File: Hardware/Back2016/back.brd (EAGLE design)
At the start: 160 x 100 mm, 12 parts, among them J1 RASPBERRYPI-40-PIN-GPIO-SMT

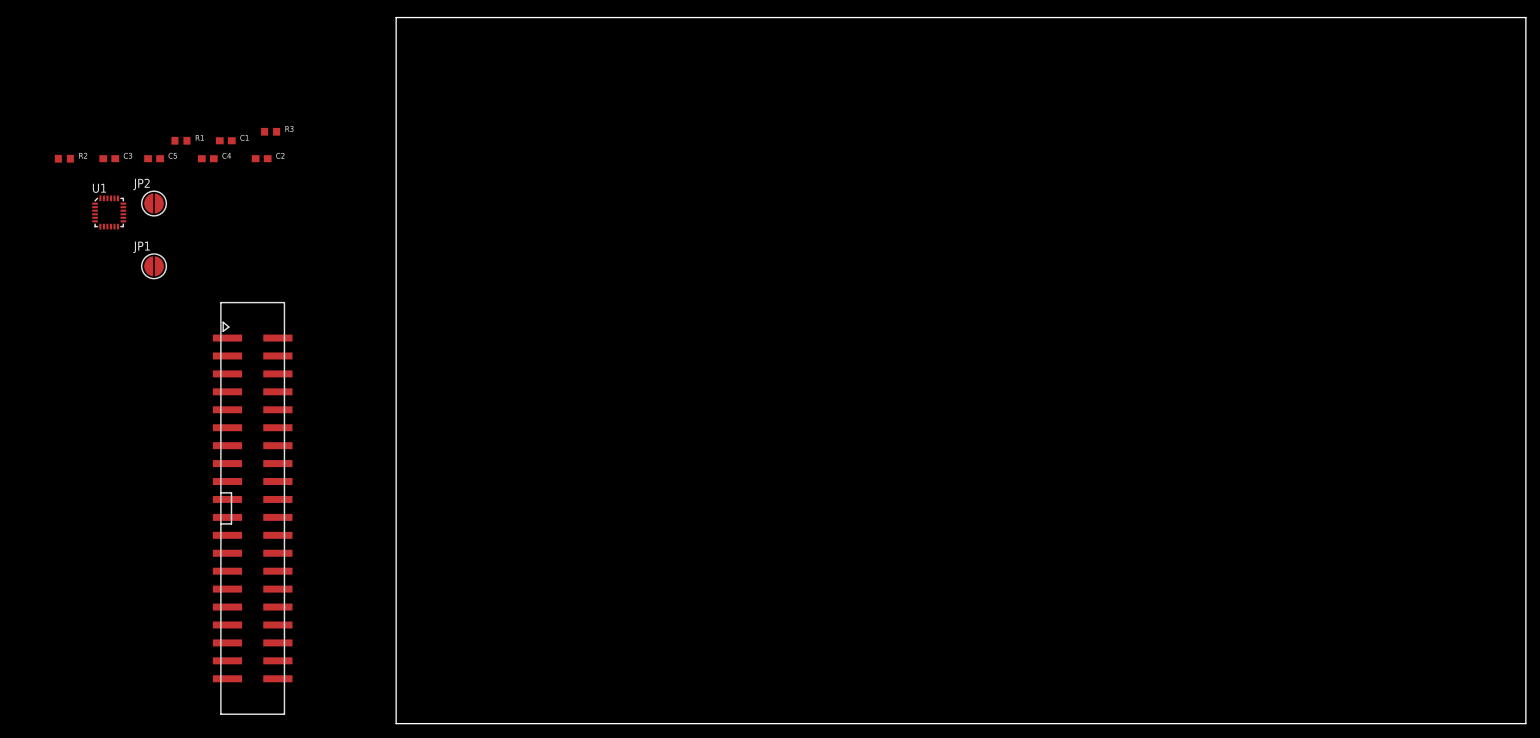
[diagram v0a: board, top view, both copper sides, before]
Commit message: Added Audio out
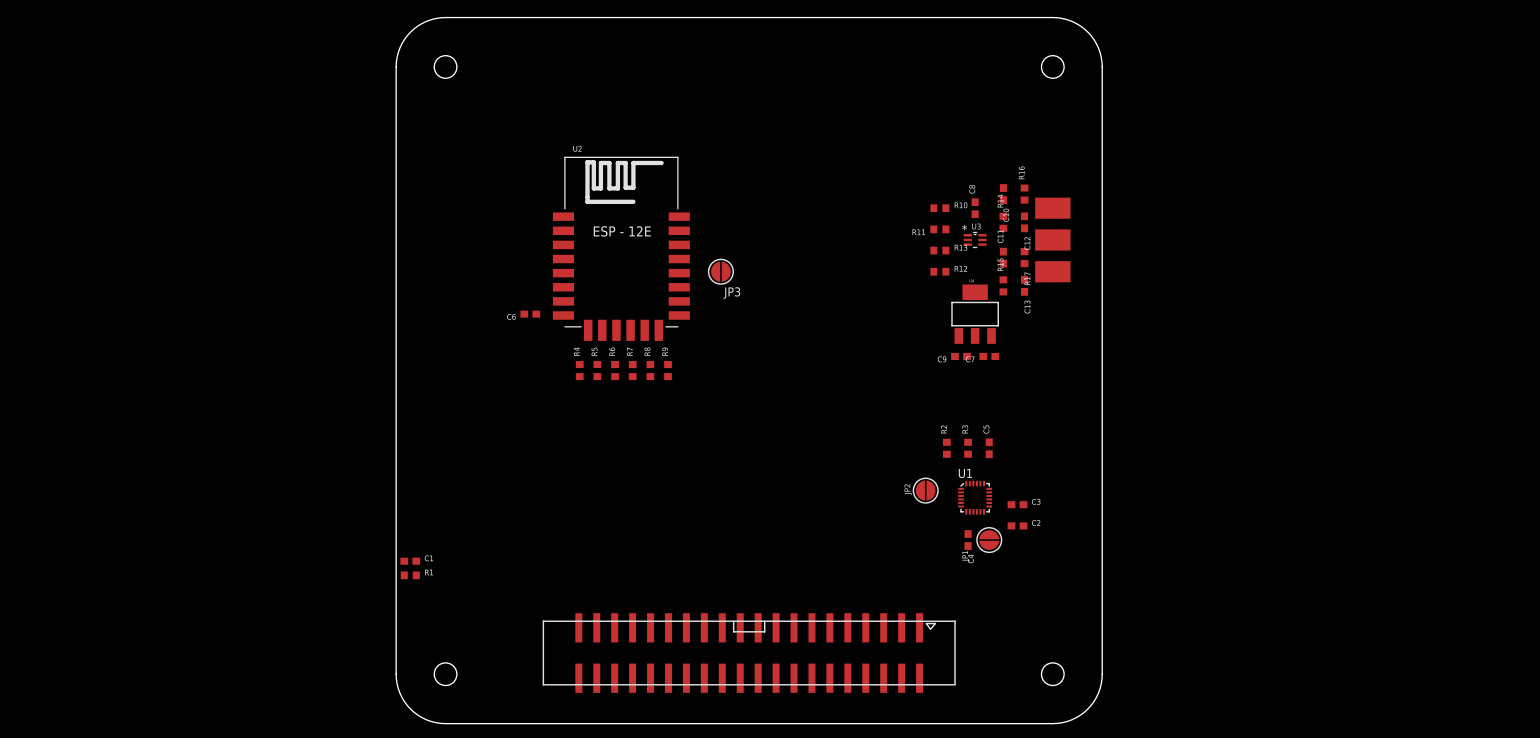
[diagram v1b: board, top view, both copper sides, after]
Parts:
- added C10, C11, C9: 100n, timearc:C0603
- added C12, C13: 47u, timearc:C0603
- added C6, C7, C8: 10u, timearc:C0603
- added JP3: JUMPER-PAD-2-NOROUND, SparkFun-Passives:PAD-JUMPER-2-NO_YES_SILK_ROUND
- added R10, R12, R14, R15, R16, R17: 100, timearc:R0603
- added R11, R13: 470, timearc:R0603
- added R4, R5, R6, R7, R8, R9: 22, timearc:R0603
- added U$1, U$2, U$3: SOLDER_PAD, timearc:SOLDER_PAD
- added U2: (no value), timearc:ESP12E-SMD
- added U3: SN74LVC2G34DCKR, timearc:SOT65P210X110-6N
- added U4: 2.5V, SparkFun-PowerIC:SOT223
- moved C3 137.7 mm to (88.0, 31.0)
- moved R2 131.5 mm to (78.0, 39.0), turned to 90 degrees
- moved U1 129.1 mm to (82.0, 32.0)
- moved C5 125.2 mm to (84.0, 39.0), turned to 90 degrees
- moved JP1 124.5 mm to (84.0, 26.0), turned to 90 degrees
- moved C4 120.5 mm to (81.0, 26.0), turned to 270 degrees
- moved C2 119.0 mm to (88.0, 28.0)
- moved JP2 116.6 mm to (75.0, 33.0)
- moved R3 108.5 mm to (81.0, 39.0), turned to 90 degrees
- moved J1 73.2 mm to (50.0, 10.0), turned to 270 degrees
- moved R1 69.6 mm to (2.00, 21.0)
- moved C1 65.0 mm to (2.00, 23.0)
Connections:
- new net 2.5V: C8.1, C9.1, U3.5, U4.2, U4.4
- new net N$10: R8.2, U2.MOSI
- new net N$11: R9.2, U2.SCLK
- new net N$12: JP3.2, U2.GPIO0
- new net N$13: R10.2, R11.1, U3.1
- new net N$14: R12.2, R13.2, U3.3
- new net N$15: R15.1, U3.4
- new net N$16: C10.2, C12.1, R14.2, R16.1
- new net N$17: C11.1, C13.1, R15.2, R17.2
- new net N$19: C12.2, U$1.1
- new net N$20: C13.2, U$2.1
- new net N$5: R14.1, U3.6
- new net N$6: R4.2, U2.CS0
- new net N$7: R5.2, U2.MISO
- new net N$8: R6.2, U2.GPIO9
- new net N$9: R7.2, U2.GPIO10
- net 3.3V: now also C6.1, U2.VCC
- net 5V: now also C7.1, U4.3
- net GND: now also C10.1, C11.2, C6.2, C7.2, C8.2, C9.2, JP3.1, R11.2, R13.1, R16.2, R17.1, U$3.1, U2.GND, U3.2, U4.1
- net ID_SD: now also U2.ADC
- net PWM0: now also R10.1
- net PWM1: now also R12.1
- net SD_CLK: now also R9.1
- net SD_CMD: now also R4.1
- net SD_D0: now also R5.1
- net SD_D1: now also R8.1
- net SD_D2: now also R6.1
- net SD_D3: now also R7.1
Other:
- board size 160 x 100 mm -> 100 x 100 mm

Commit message: Added Teensy LC SMD version
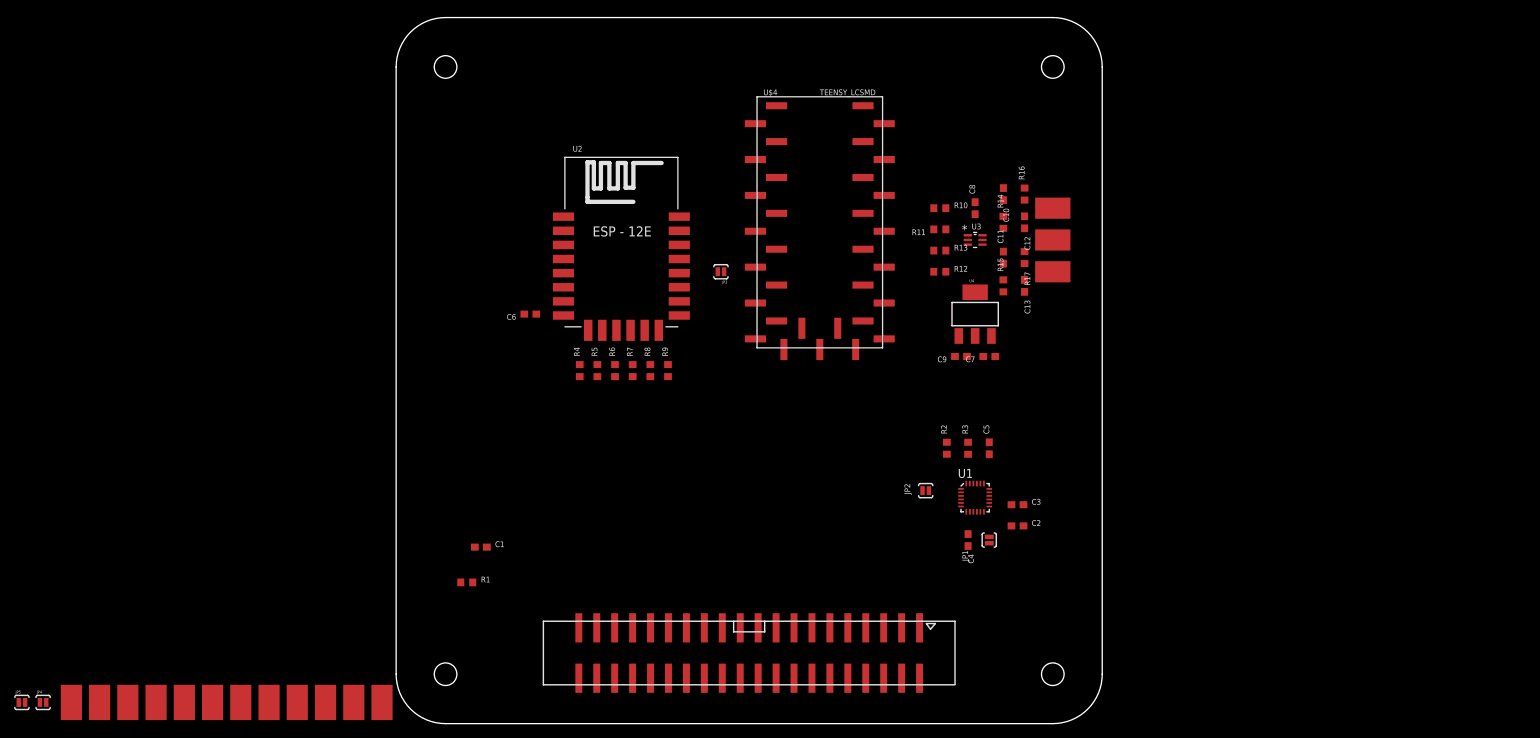
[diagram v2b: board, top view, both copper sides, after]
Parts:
- added JP4, JP5: JUMPER-PAD-2-NOYES_SILK, SparkFun-Passives:PAD-JUMPER-2-NO_YES_SILK
- added RX3, TX3, U$10, U$11, U$12, U$13, U$14, U$5, U$6, U$7, U$8, U$9: SOLDER_PAD, timearc:SOLDER_PAD
- added U$4: TEENSY_LCSMD, timearc:TEENSY_LC_SMD
- JP1, JP2, JP3: value JUMPER-PAD-2-NOROUND -> JUMPER-PAD-2-NOYES_SILK; device SparkFun-Passives:PAD-JUMPER-2-NO_YES_SILK_ROUND -> SparkFun-Passives:PAD-JUMPER-2-NO_YES_SILK
- U1: device SparkFun-Sensors:QFN-24-NP -> timearc:QFN-24-NP
- moved C1 10.2 mm to (12.0, 25.0)
- moved R1 8.06 mm to (10.0, 20.0)
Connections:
- new net N$21: U$4.P0, U$5.1
- new net N$22: U$4.P1, U$6.1
- new net N$23: U$4.P3, U$7.1
- new net N$24: U$4.P4, U$8.1
- new net N$25: U$4.P23, U$9.1
- new net N$26: U$10.1, U$4.P22
- new net N$27: JP4.2, U$11.1, U$4.P19
- new net N$28: JP5.2, U$12.1, U$4.P18
- new net N$29: U$13.1, U$4.P16
- new net N$30: U$14.1, U$4.P15
- new net N$31: RX3.1, U$4.P7
- new net N$32: TX3.1, U$4.P8
- new net WS2812: U$4.P17_5V
- net 5V: now also U$4.VIN
- net GND: now also U$4.GND@1, U$4.GND@2, U$4.GND@3
- net SCL: now also JP5.1
- net SDA: now also JP4.1
- net UART_RX: now also U$4.P10
- net UART_TX: now also U$4.P9

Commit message: Start routing board Back2016/back.brd Added keep out to Front2014/uac.brd Tweaked the 3d print design
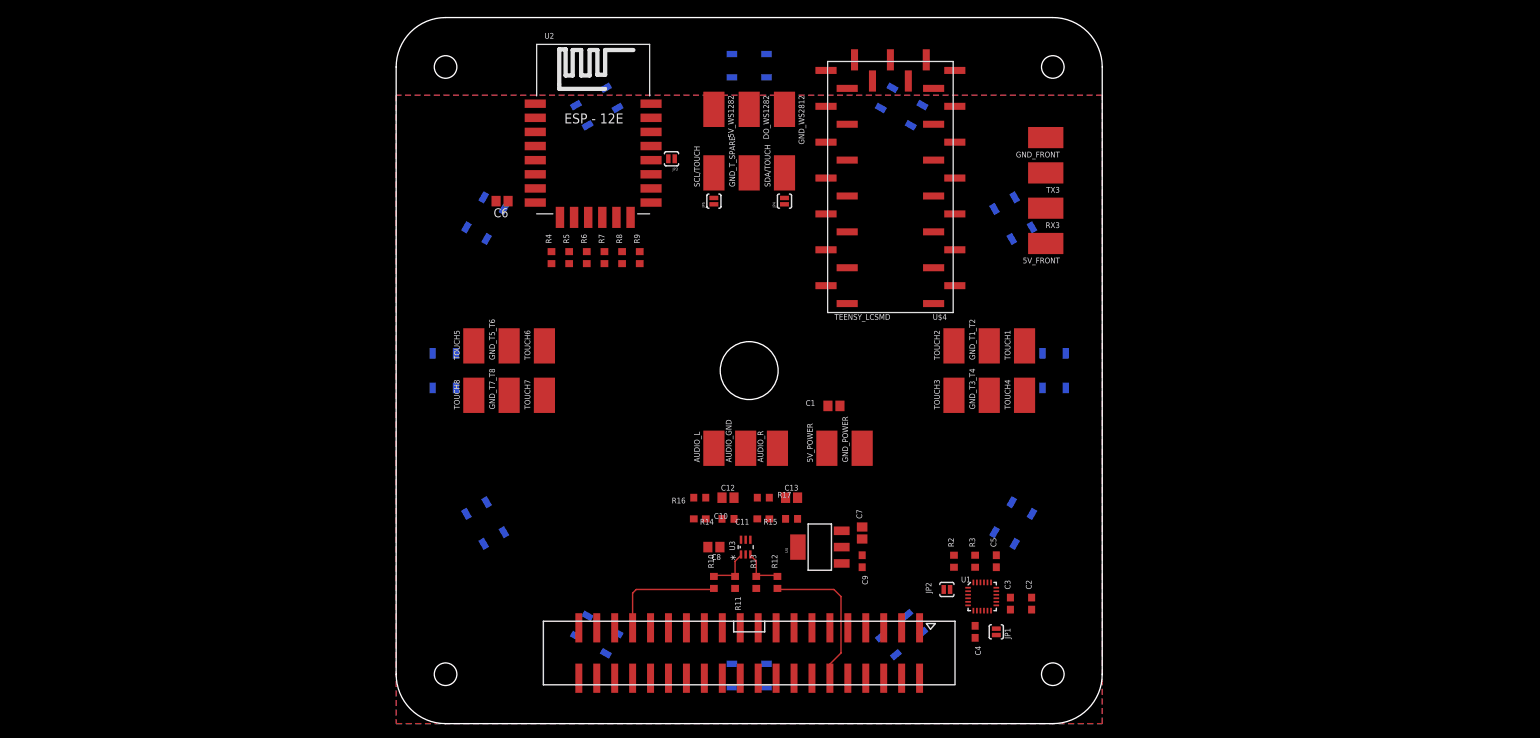
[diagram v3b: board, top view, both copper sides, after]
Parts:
- removed R1: (no value), timearc:R0603
- removed U$1, U$10, U$11, U$12, U$13, U$14, U$2, U$3, U$5, U$6, U$7, U$8, U$9: SOLDER_PAD, timearc:SOLDER_PAD
- added 5V_FRONT, 5V_POWER, 5V_WS1282, AUDIO_GND, AUDIO_L, AUDIO_R, DO_WS1282, GND_FRONT, GND_POWER, GND_T1_T2, GND_T3_T4, GND_T5_T6, GND_T7_T8, GND_T_SPARE, GND_WS2812, SCL/TOUCH, SDA/TOUCH, TOUCH1, TOUCH2, TOUCH3, TOUCH4, TOUCH5, TOUCH6, TOUCH7, TOUCH8: SOLDER_PAD, timearc:SOLDER_PAD
- added LED1, LED10, LED11, LED12, LED2, LED3, LED4, LED5, LED6, LED7, LED8, LED9: WS2812B5050, adafruit:WS2812B
- added U$15: (no value), timearc:TIMEARC_KEEPOUT
- C1: value (none) -> 10u; device timearc:C0603 -> timearc:C0805
- C12, C13, C6, C7, C8: device timearc:C0603 -> timearc:C0805
- moved TX3 157.1 mm to (92.0, 78.0), turned to 90 degrees
- moved RX3 151.2 mm to (92.0, 73.0), turned to 90 degrees
- moved JP4 126.8 mm to (55.0, 74.0), turned to 90 degrees
- moved JP5 121.0 mm to (45.0, 74.0), turned to 90 degrees
- moved C10 63.0 mm to (43.0, 29.0), turned to 0 degrees
- moved R16 63.0 mm to (43.0, 32.0), turned to 180 degrees
- moved R10 61.9 mm to (45.0, 20.0), turned to 90 degrees
- moved C8 60.6 mm to (45.0, 25.0), turned to 180 degrees
- moved R11 57.8 mm to (48.0, 20.0), turned to 270 degrees
- moved C12 57.3 mm to (47.0, 32.0), turned to 0 degrees
- moved R14 57.3 mm to (47.0, 29.0), turned to 180 degrees
- moved U3 54.3 mm to (49.5, 25.0), turned to 90 degrees
- moved C1 53.9 mm to (62.0, 45.0)
- moved R13 53.7 mm to (51.0, 20.0), turned to 90 degrees
- moved C11 50.2 mm to (52.0, 29.0), turned to 180 degrees
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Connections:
- new net N$18: LED1.2-DOUT, LED2.4-DIN
- new net N$33: LED2.2-DOUT, LED3.4-DIN
- new net N$34: LED3.2-DOUT, LED4.4-DIN
- new net N$35: LED4.2-DOUT, LED5.4-DIN
- new net N$36: LED5.2-DOUT, LED6.4-DIN
- new net N$37: LED6.2-DOUT, LED7.4-DIN
- new net N$38: LED7.2-DOUT, LED8.4-DIN
- new net N$39: LED8.2-DOUT, LED9.4-DIN
- new net N$40: LED10.4-DIN, LED9.2-DOUT
- new net N$41: LED10.2-DOUT, LED11.4-DIN
- new net N$42: LED11.2-DOUT, LED12.4-DIN
- new net N$43: DO_WS1282.1, LED12.2-DOUT
- net 5V: now also 5V_FRONT.1, 5V_POWER.1, 5V_WS1282.1, C1.1, LED1.1-VDD, LED10.1-VDD, LED11.1-VDD, LED12.1-VDD, LED2.1-VDD, LED3.1-VDD, LED4.1-VDD, LED5.1-VDD, LED6.1-VDD, LED7.1-VDD, LED8.1-VDD, LED9.1-VDD
- net GND: now also AUDIO_GND.1, C1.2, GND_FRONT.1, GND_POWER.1, GND_T1_T2.1, GND_T3_T4.1, GND_T5_T6.1, GND_T7_T8.1, GND_T_SPARE.1, GND_WS2812.1, LED1.3-GND, LED10.3-GND, LED11.3-GND, LED12.3-GND, LED2.3-GND, LED3.3-GND, LED4.3-GND, LED5.3-GND, LED6.3-GND, LED7.3-GND, LED8.3-GND, LED9.3-GND; no longer U$3.1
- net N$19: now also AUDIO_L.1; no longer U$1.1
- net N$20: now also AUDIO_R.1; no longer U$2.1
- net N$21: now also TOUCH1.1; no longer U$5.1
- net N$22: now also TOUCH2.1; no longer U$6.1
- net N$23: now also TOUCH3.1; no longer U$7.1
- net N$24: now also TOUCH4.1; no longer U$8.1
- net N$25: now also TOUCH5.1; no longer U$9.1
- net N$26: now also TOUCH6.1; no longer U$10.1
- net N$27: now also SDA/TOUCH.1; no longer U$11.1
- net N$28: now also SCL/TOUCH.1; no longer U$12.1
- net N$29: now also TOUCH7.1; no longer U$13.1
- net N$30: now also TOUCH8.1; no longer U$14.1
- net PWM0: now also R12.1; no longer R10.1
- net PWM1: now also R10.1; no longer R12.1
- net WS2812: now also LED1.4-DIN
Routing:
- net PWM0: track 0.00 -> 21.7 mm
- net PWM1: track 0.00 -> 16.7 mm
- net N$14: track 0.00 -> 6.67 mm
- net N$13: track 0.00 -> 6.67 mm
- added copper zone on layer 16, net +5V
- added copper zone on layer 1, net GND

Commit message: 100% connected
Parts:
- added C14, C15: 10u, timearc:C0805
- added JP6, JP7: JUMPER-PAD-2-NOYES_SILK, SparkFun-Passives:PAD-JUMPER-2-NO_YES_SILK
- added U5: 3.3V, SparkFun-PowerIC:SOT223
- moved C6 57.2 mm to (34.0, 20.0), turned to 0 degrees
- moved U2 53.9 mm to (18.0, 29.0), turned to 90 degrees
- moved R4 44.6 mm to (34.0, 23.0), turned to 180 degrees
- moved JP3 44.3 mm to (20.0, 40.0), turned to 270 degrees
- moved R5 41.6 mm to (34.0, 25.5), turned to 180 degrees
- moved R6 38.6 mm to (34.0, 28.0), turned to 180 degrees
- moved R7 35.8 mm to (34.0, 30.5), turned to 180 degrees
- moved TOUCH4 34.4 mm to (67.0, 73.0)
- moved R8 33.1 mm to (34.0, 33.0), turned to 180 degrees
- moved C2 31.1 mm to (88.0, 48.0), turned to 180 degrees
- moved JP1 30.8 mm to (92.0, 43.0), turned to 180 degrees
- moved R9 30.5 mm to (34.0, 35.5), turned to 180 degrees
- moved 5V_FRONT 29.2 mm to (67.0, 83.0), turned to 180 degrees
- moved GND_T3_T4 29.1 mm to (72.0, 73.0)
- moved GND_T7_T8 29.1 mm to (28.0, 73.0)
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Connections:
- new net 3.3V_RPI: J1.1, J1.17, JP7.1
- new net N$44: C15.1, JP6.1, U5.2, U5.4
- net 3.3V: now also JP6.2, JP7.2; no longer J1.1, J1.17
- net 5V: now also C14.1, U5.3
- net GND: now also C14.2, C15.2, U5.1
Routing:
- net SDA: track 0.00 -> 162.2 mm, vias 0 -> 8
- net 3.3V: track 0.00 -> 159.1 mm, vias 0 -> 6
- net SCL: track 0.00 -> 154.0 mm, vias 0 -> 6
- net UART_TX: track 0.00 -> 107.8 mm, vias 0 -> 2
- net UART_RX: track 0.00 -> 107.5 mm, vias 0 -> 2
- net GND: track 0.00 -> 82.2 mm, vias 0 -> 14
- net 5V: track 0.00 -> 67.9 mm, vias 0 -> 7
- net SD_CMD: track 0.00 -> 44.7 mm, vias 0 -> 2
- net N$28: track 0.00 -> 43.6 mm
- net SD_CLK: track 0.00 -> 43.1 mm, vias 0 -> 2
- net SD_D3: track 0.00 -> 41.0 mm, vias 0 -> 2
- net SD_D1: track 0.00 -> 39.7 mm, vias 0 -> 2
- net ID_SD: track 0.00 -> 39.1 mm, vias 0 -> 2
- net N$27: track 0.00 -> 36.6 mm
- net SD_D0: track 0.00 -> 36.4 mm, vias 0 -> 2
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- added copper zone on layer 16, net 5V
- removed copper zone on layer 16, net +5V

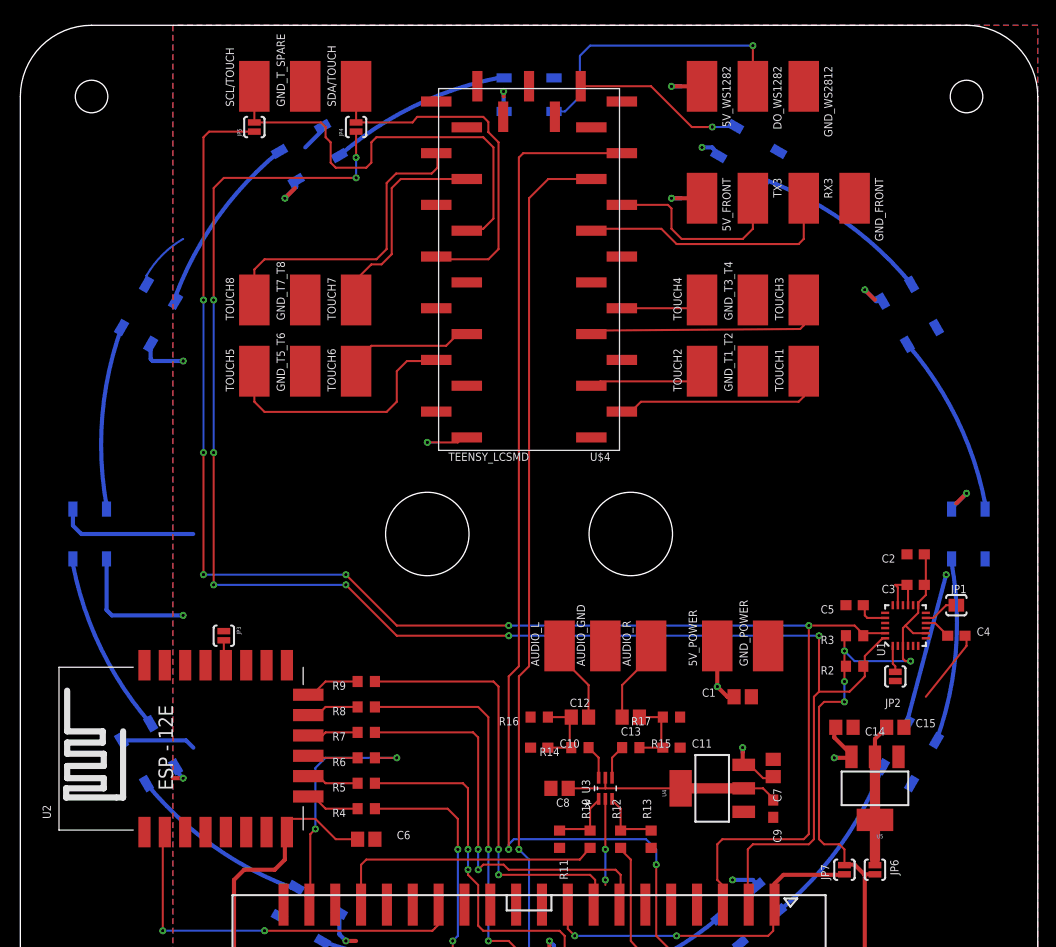
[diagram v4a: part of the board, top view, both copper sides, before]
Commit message: Tweaked the silk screen
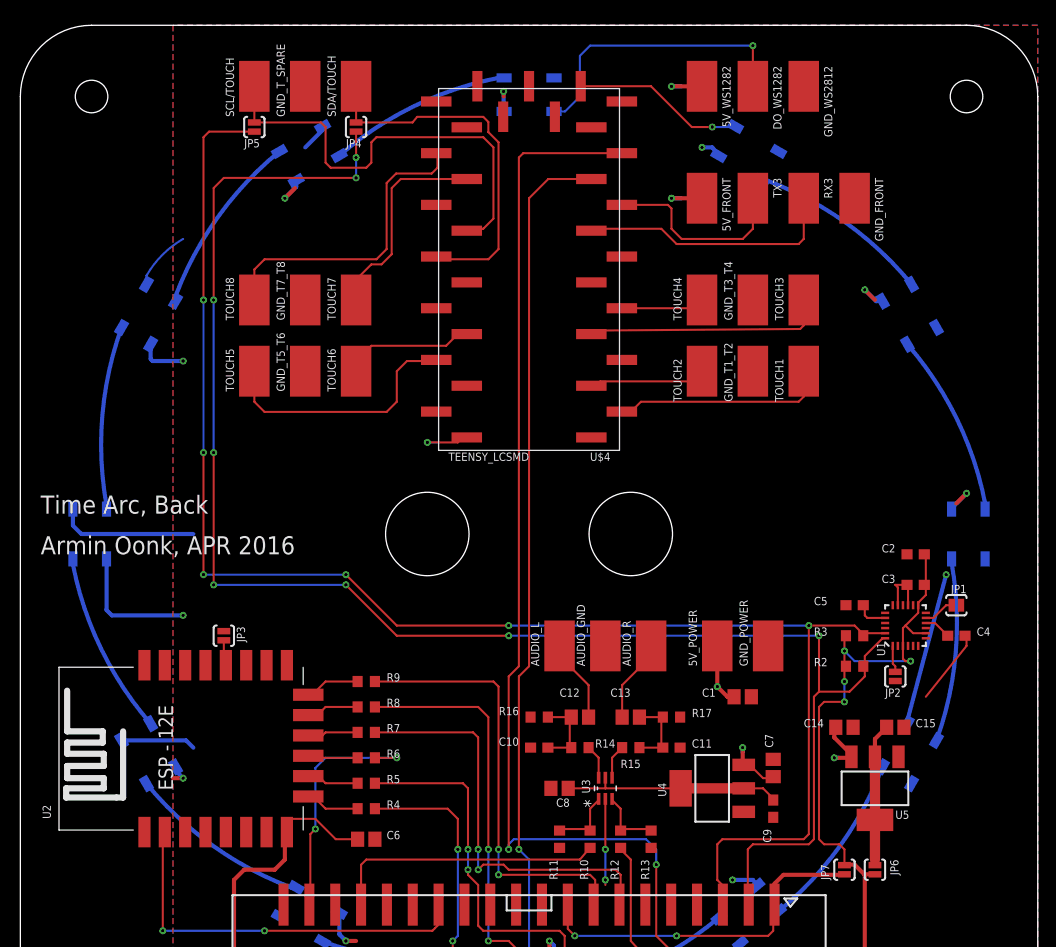
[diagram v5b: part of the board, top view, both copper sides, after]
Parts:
- LED1, LED10, LED11, LED12, LED2, LED3, LED4, LED5, LED6, LED7, LED8, LED9: device adafruit:WS2812B -> timearc:WS2812B
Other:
- board text added: "Armin Oonk, APR 2016"
- board text added: "Time Arc, Back"
